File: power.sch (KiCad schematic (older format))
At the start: 33 parts, among them J2 4DB-P108-06, J3 39531-1002, J4 39531-1002, U2 i3A, U3 AP7365-33WG-7

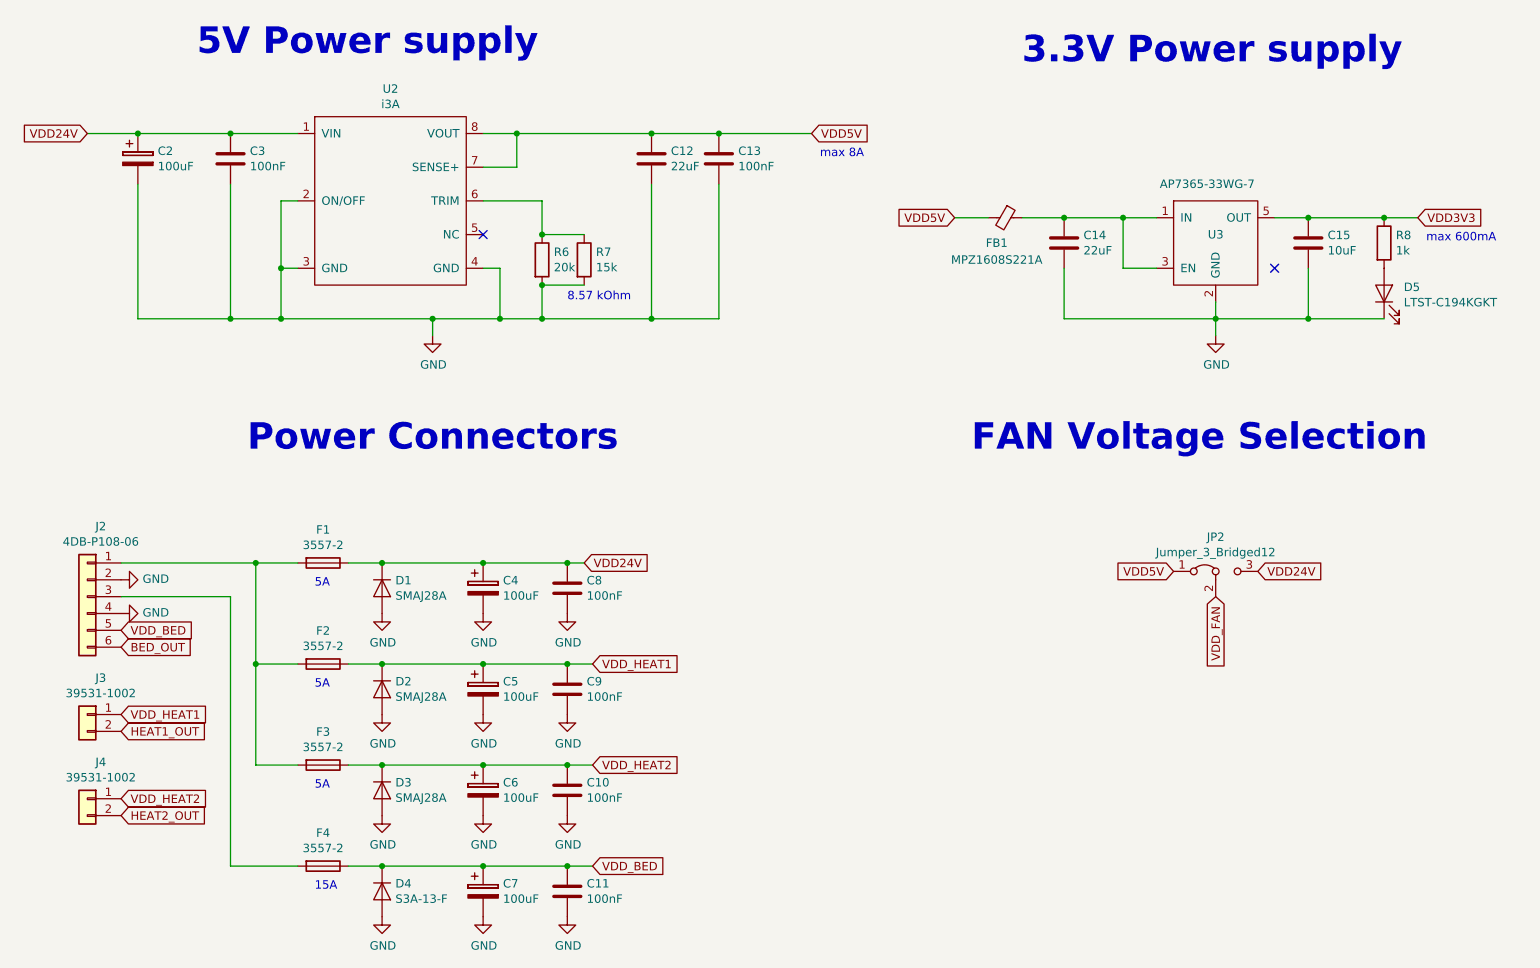
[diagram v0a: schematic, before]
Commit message: Updated board to version 1.2
 * Switched small MOSFETs to SOT-23 package
 * Redesigned TMC*160 driver layout
 * Changed 01x03 to 02x03 jumper for FAN voltage selection
 * Switches STATUS_LED pin
 * Some copper pour optimizations
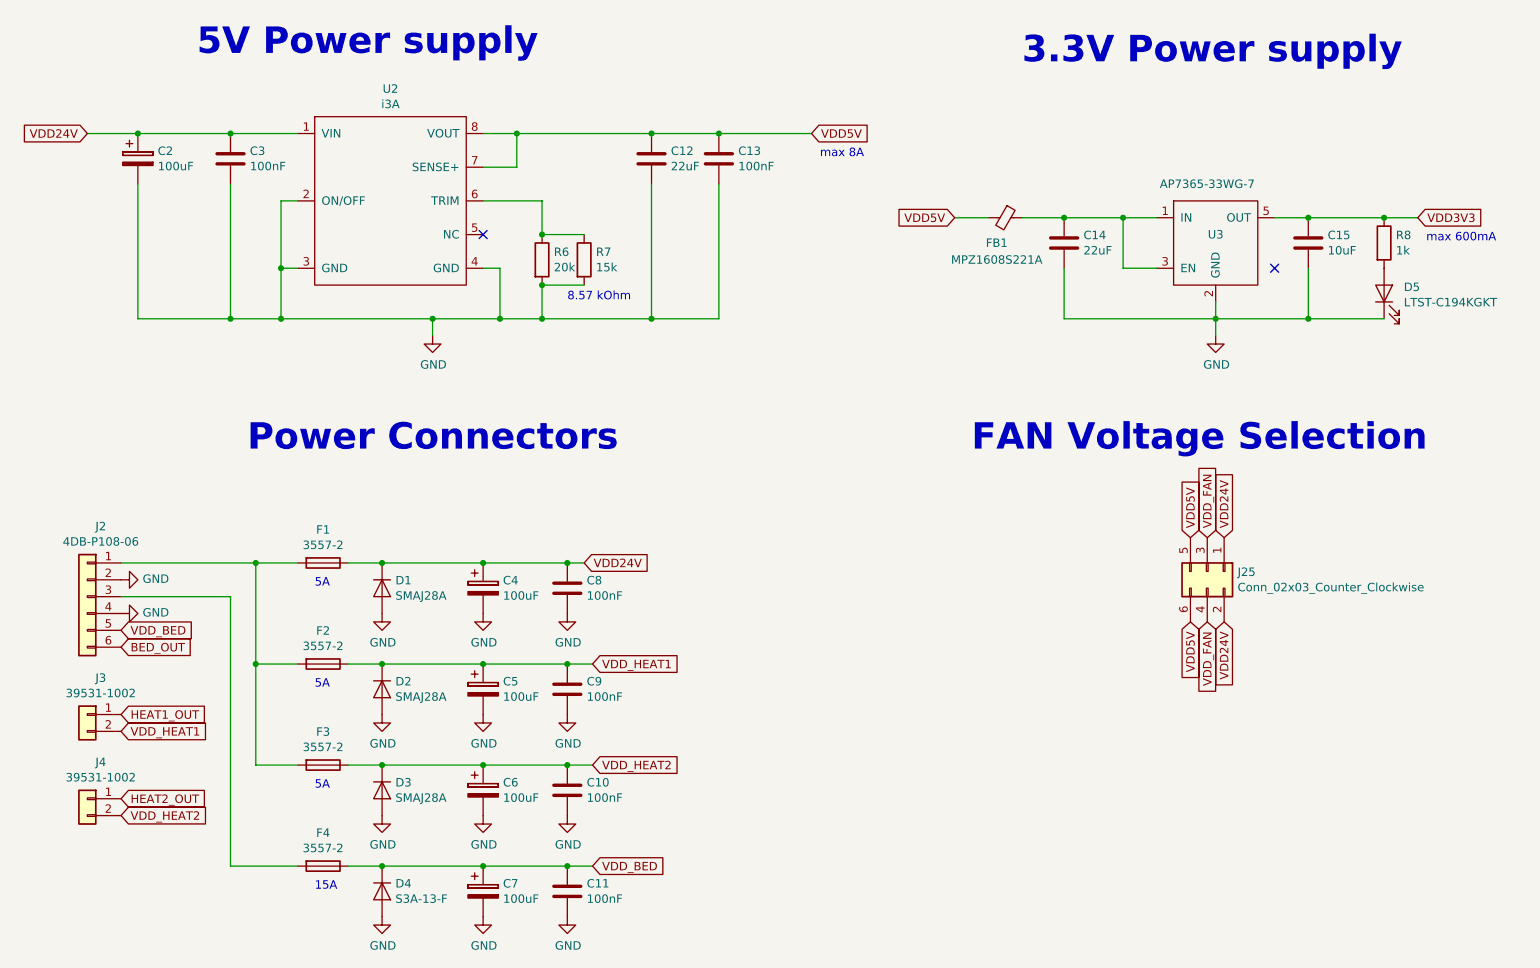
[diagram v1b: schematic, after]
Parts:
- removed JP2: Jumper_3_Bridged12, Connector_PinHeader_2.54mm:PinHeader_1x03_P2.54mm_Vertical, symbol Jumper:Jumper_3_Bridged12
- added J25: Conn_02x03_Counter_Clockwise, Connector_PinHeader_2.54mm:PinHeader_2x03_P2.54mm_Vertical, symbol Connector_Generic:Conn_02x03_Odd_Even
- C2, C4, C5, C6, C7: footprint Capacitor_SMD:CP_Elec_6.3x5.7 -> Capacitor_THT:CP_Radial_D6.3mm_P2.50mm
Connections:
- net HEAT1_OUT: now also J3.1 (Pin_1); no longer J3.2 (Pin_2)
- net HEAT2_OUT: now also J4.1 (Pin_1); no longer J4.2 (Pin_2)
- net VDD24V: now also J25.1 (Pin_1), J25.2 (Pin_2)
- net VDD5V: now also J25.5 (Pin_5), J25.6 (Pin_6)
- net VDD_FAN: now also J25.3 (Pin_3), J25.4 (Pin_4)
- net VDD_HEAT1: now also J3.2 (Pin_2); no longer J3.1 (Pin_1)
- net VDD_HEAT2: now also J4.2 (Pin_2); no longer J4.1 (Pin_1)
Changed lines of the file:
@@
 F 0 "C2" H 1618 1446 50  0000 L CNN
 F 1 "100uF" H 1618 1355 50  0000 L CNN
-F 2 "Capacitor_SMD:CP_Elec_6.3x5.7" H 1538 1250 50  0001 C CNN
+F 2 "Capacitor_THT:CP_Radial_D6.3mm_P2.50mm" H 1538 1250 50  0001 C CNN
 F 3 "" H 1500 1400 50  0001 C CNN
 	1    1500 1400
@@
 F 0 "C6" H 3668 5196 50  0000 L CNN
 F 1 "100uF" H 3668 5105 50  0000 L CNN
-F 2 "Capacitor_SMD:CP_Elec_6.3x5.7" H 3588 5000 50  0001 C CNN
+F 2 "Capacitor_THT:CP_Radial_D6.3mm_P2.50mm" H 3588 5000 50  0001 C CNN
 F 3 "" H 3550 5150 50  0001 C CNN
 	1    3550 5150
@@
 F 0 "C5" H 3668 4596 50  0000 L CNN
 F 1 "100uF" H 3668 4505 50  0000 L CNN
-F 2 "Capacitor_SMD:CP_Elec_6.3x5.7" H 3588 4400 50  0001 C CNN
+F 2 "Capacitor_THT:CP_Radial_D6.3mm_P2.50mm" H 3588 4400 50  0001 C CNN
 F 3 "" H 3550 4550 50  0001 C CNN
 	1    3550 4550
@@
 F 0 "C4" H 3668 3996 50  0000 L CNN
 F 1 "100uF" H 3668 3905 50  0000 L CNN
-F 2 "Capacitor_SMD:CP_Elec_6.3x5.7" H 3588 3800 50  0001 C CNN
+F 2 "Capacitor_THT:CP_Radial_D6.3mm_P2.50mm" H 3588 3800 50  0001 C CNN
 F 3 "" H 3550 3950 50  0001 C CNN
 	1    3550 3950
@@
 F 0 "C7" H 3668 5796 50  0000 L CNN
 F 1 "100uF" H 3668 5705 50  0000 L CNN
-F 2 "Capacitor_SMD:CP_Elec_6.3x5.7" H 3588 5600 50  0001 C CNN
+F 2 "Capacitor_THT:CP_Radial_D6.3mm_P2.50mm" H 3588 5600 50  0001 C CNN
 F 3 "" H 3550 5750 50  0001 C CNN
 	1    3550 5750
@@
 Text GLabel 1400 4200 2    50   Input ~ 0
 VDD_BED
-Text GLabel 1400 4700 2    50   Input ~ 0
+Text GLabel 1400 4800 2    50   Input ~ 0
 VDD_HEAT1
-Text GLabel 1400 5200 2    50   Input ~ 0
+Text GLabel 1400 5300 2    50   Input ~ 0
 VDD_HEAT2
 Text GLabel 1400 4300 2    50   Input ~ 0
 BED_OUT
-Text GLabel 1400 4800 2    50   Input ~ 0
+Text GLabel 1400 4700 2    50   Input ~ 0
 HEAT1_OUT
-Text GLabel 1400 5300 2    50   Input ~ 0
+Text GLabel 1400 5200 2    50   Input ~ 0
 HEAT2_OUT
-$Comp
-L Jumper:Jumper_3_Bridged12 JP2
-U 1 1 5BC68888
-P 7900 3850
-F 0 "JP2" H 7900 4054 50  0000 C CNN
-F 1 "Jumper_3_Bridged12" H 7900 3963 50  0000 C CNN
-F 2 "Connector_PinHeader_2.54mm:PinHeader_1x03_P2.54mm_Vertical" H 7900 3850 50  0001 C CNN
-F 3 "~" H 7900 3850 50  0001 C CNN
-	1    7900 3850
-	1    0    0    -1
-$EndComp
-Text GLabel 7650 3850 0    50   Input ~ 0
+Text GLabel 7750 3650 1    50   Input ~ 0
 VDD5V
-Text GLabel 8150 3850 2    50   Input ~ 0
+Text GLabel 7950 3650 1    50   Input ~ 0
 VDD24V
-Text GLabel 7900 4000 3    50   Input ~ 0
+Text GLabel 7850 4150 3    50   Input ~ 0
 VDD_FAN
 Text Notes 6450 3150 0    157  ~ 31
@@
 Wire Wire Line
 	8450 1750 8900 1750
+$Comp
+L Connector_Generic:Conn_02x03_Odd_Even J25
+U 1 1 5C045A3C
+P 7850 3850
+F 0 "J25" V 7854 4030 50  0000 L CNN
+F 1 "Conn_02x03_Counter_Clockwise" V 7945 4030 50  0000 L CNN
+F 2 "Connector_PinHeader_2.54mm:PinHeader_2x03_P2.54mm_Vertical" H 7850 3850 50  0001 C CNN
+F 3 "~" H 7850 3850 50  0001 C CNN
+	1    7850 3850
+	0    1    1    0
+$EndComp
+Text GLabel 7850 3650 1    50   Input ~ 0
+VDD_FAN
+Text GLabel 7750 4150 3    50   Input ~ 0
+VDD5V
+Text GLabel 7950 4150 3    50   Input ~ 0
+VDD24V
 $EndSCHEMATC

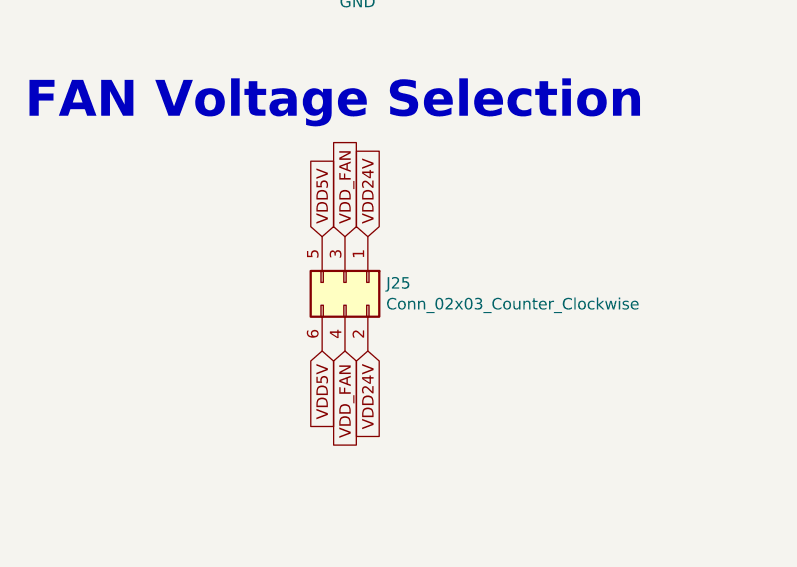
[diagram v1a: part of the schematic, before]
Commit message: Add PU for SD_DETECT_PIN
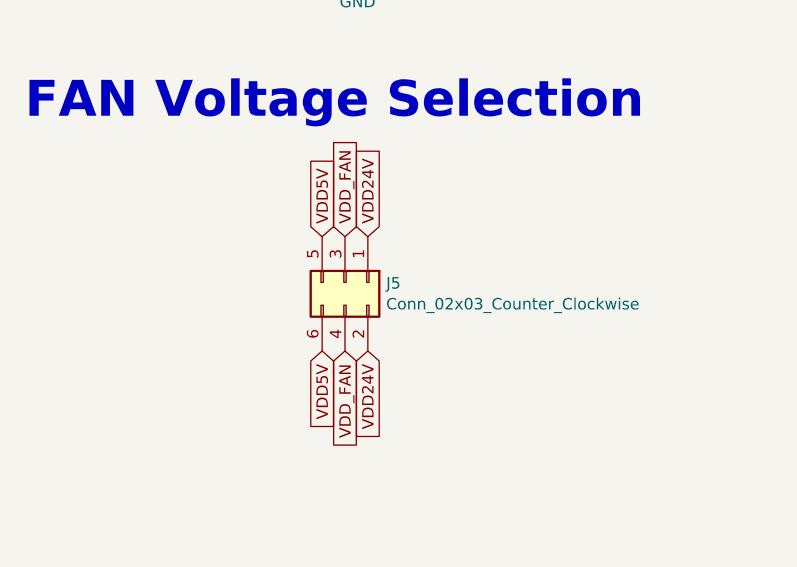
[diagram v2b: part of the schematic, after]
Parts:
- renumbered J25 to J5
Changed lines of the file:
@@
 	8450 1750 8900 1750
 $Comp
-L Connector_Generic:Conn_02x03_Odd_Even J25
+L Connector_Generic:Conn_02x03_Odd_Even J5
 U 1 1 5C045A3C
 P 7850 3850
-F 0 "J25" V 7854 4030 50  0000 L CNN
+F 0 "J5" V 7854 4030 50  0000 L CNN
 F 1 "Conn_02x03_Counter_Clockwise" V 7945 4030 50  0000 L CNN
 F 2 "Connector_PinHeader_2.54mm:PinHeader_2x03_P2.54mm_Vertical" H 7850 3850 50  0001 C CNN

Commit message: Improve Readability
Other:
- moved on the sheet: FB1, J5
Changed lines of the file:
@@
 L Device:Ferrite_Bead_Small FB?
 U 1 1 5BCC4BBE
-P 6650 1750
+P 6700 1750
 AR Path="/5BC1C8A4/5BCC4BBE" Ref="FB?"  Part="1"
 AR Path="/5BC54251/5BCC4BBE" Ref="FB1"  Part="1"
-F 0 "FB1" V 6800 1700 50  0000 C CNN
-F 1 "MPZ1608S221A" V 6900 1700 50  0000 C CNN
-F 2 "Resistor_SMD:R_0603_1608Metric" V 6580 1750 50  0001 C CNN
-F 3 "https://www.mouser.de/datasheet/2/400/eads_commercial_power_mpz1608_en-923650.pdf" H 6650 1750 50  0001 C CNN
-	1    6650 1750
+F 0 "FB1" V 6850 1700 50  0000 C CNN
+F 1 "MPZ1608S221A" V 6950 1700 50  0000 C CNN
+F 2 "Resistor_SMD:R_0603_1608Metric" V 6630 1750 50  0001 C CNN
+F 3 "https://www.mouser.de/datasheet/2/400/eads_commercial_power_mpz1608_en-923650.pdf" H 6700 1750 50  0001 C CNN
+	1    6700 1750
 	0    1    1    0
 $EndComp
 Wire Wire Line
-	6350 1750 6550 1750
+	6350 1750 6600 1750
 $Comp
 L Device:C C15
@@
 Connection ~ 8450 1750
 Wire Wire Line
-	6750 1750 7000 1750
+	6800 1750 7000 1750
 Connection ~ 7000 1750
 Connection ~ 7350 1750
@@
 Text GLabel 1400 5200 2    50   Input ~ 0
 HEAT2_OUT
-Text GLabel 7750 3650 1    50   Input ~ 0
+Text GLabel 7550 3850 0    50   Input ~ 0
 VDD5V
-Text GLabel 7950 3650 1    50   Input ~ 0
+Text GLabel 7550 3650 0    50   Input ~ 0
 VDD24V
-Text GLabel 7850 4150 3    50   Input ~ 0
+Text GLabel 8050 3750 2    50   Input ~ 0
 VDD_FAN
 Text Notes 6450 3150 0    157  ~ 31
@@
 L Connector_Generic:Conn_02x03_Odd_Even J5
 U 1 1 5C045A3C
-P 7850 3850
-F 0 "J5" V 7854 4030 50  0000 L CNN
-F 1 "Conn_02x03_Counter_Clockwise" V 7945 4030 50  0000 L CNN
-F 2 "Connector_PinHeader_2.54mm:PinHeader_2x03_P2.54mm_Vertical" H 7850 3850 50  0001 C CNN
-F 3 "~" H 7850 3850 50  0001 C CNN
-	1    7850 3850
-	0    1    1    0
-$EndComp
-Text GLabel 7850 3650 1    50   Input ~ 0
+P 7750 3750
+F 0 "J5" H 7750 4100 50  0000 L CNN
+F 1 "Conn_02x03_Counter_Clockwise" H 7200 4000 50  0000 L CNN
+F 2 "Connector_PinHeader_2.54mm:PinHeader_2x03_P2.54mm_Vertical" H 7750 3750 50  0001 C CNN
+F 3 "~" H 7750 3750 50  0001 C CNN
+	1    7750 3750
+	1    0    0    -1
+$EndComp
+Text GLabel 7550 3750 0    50   Input ~ 0
 VDD_FAN
-Text GLabel 7750 4150 3    50   Input ~ 0
+Text GLabel 8050 3850 2    50   Input ~ 0
 VDD5V
-Text GLabel 7950 4150 3    50   Input ~ 0
+Text GLabel 8050 3650 2    50   Input ~ 0
 VDD24V
 $EndSCHEMATC
